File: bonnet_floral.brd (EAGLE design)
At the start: 65 x 30 mm, 10 parts, among them IC1 RASPBERRY_PI_ZERO_W_(V1.3)-WO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

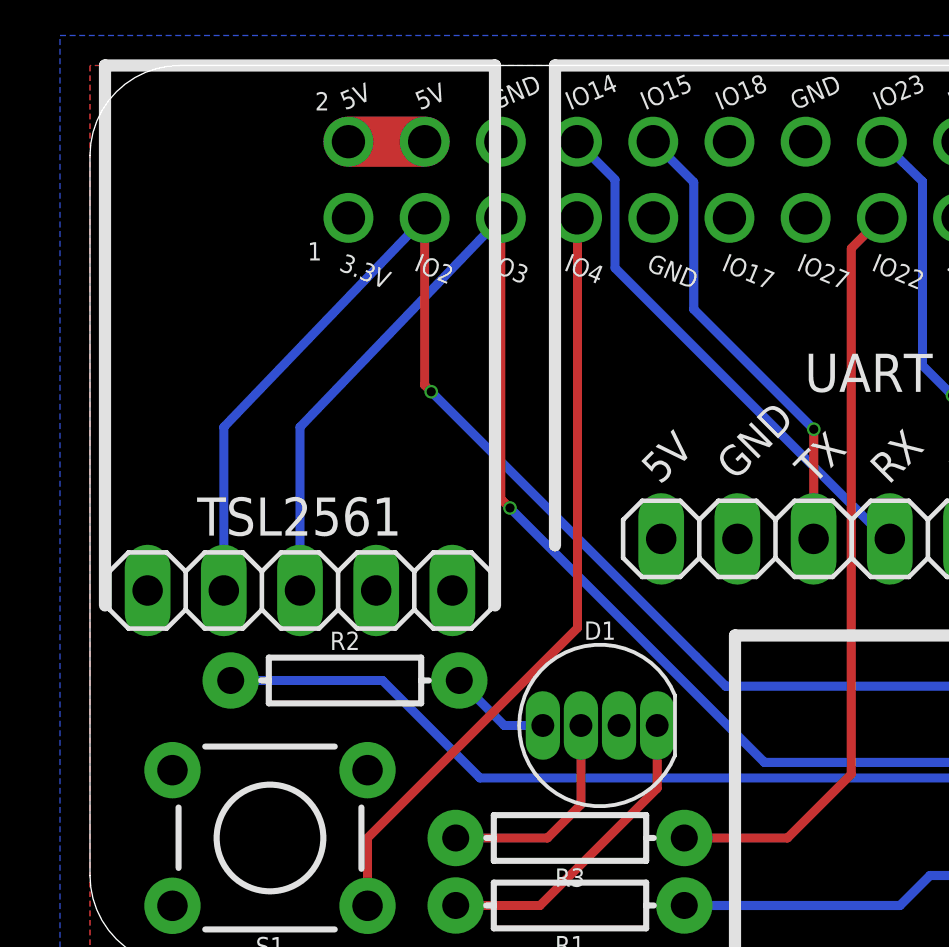
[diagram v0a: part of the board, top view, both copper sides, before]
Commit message: Adjusting the back silkscreen, adding artwork
Also cleaning up the DRC checks from before
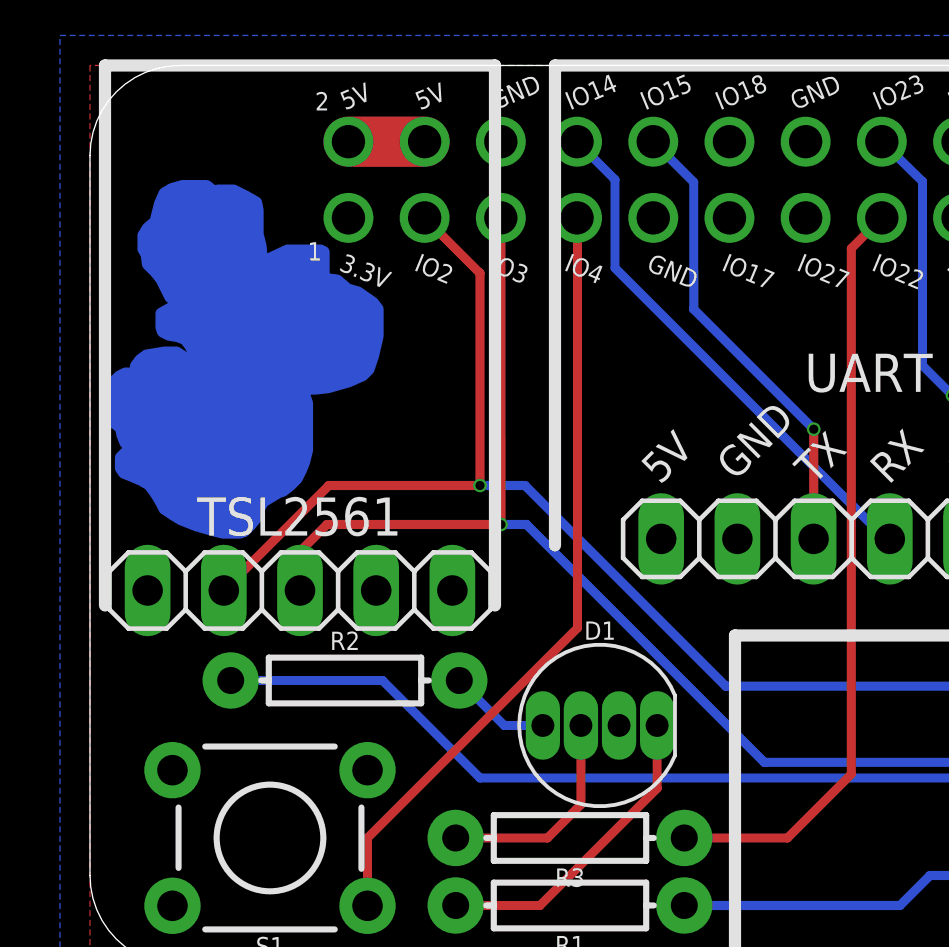
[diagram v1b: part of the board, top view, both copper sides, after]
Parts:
- added U$1: (no value), Artwork:FLORAL_SMALLER_MIRROR
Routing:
- net I2C_SCL: track 48.9 -> 42.7 mm
- net I2C_SDA: track 48.2 -> 43.9 mm
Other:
- board text added: "Floral Bonnet V0.9.1 John 'Warthog9' Hawley (C) 2018 CC-BY-SA 4.0"
- board text added: "https://github.com/unreproducible/bonnet_floral"
- board text removed: "Floral Bonnet V0.9.1 John 'Warthog9' Hawley (C) 2018 CC-BY-SA 4.0 https://github.com/unreproducible/bonnet_floral"
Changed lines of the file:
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@@
 <setting verticaltext="up"/>
 </settings>
-<grid distance="1" unitdist="mm" unit="mm" style="lines" multiple="1" display="no" altdistance="0.5" altunitdist="mm" altunit="mm"/>
+<grid distance="0.0025" unitdist="inch" unit="inch" style="lines" multiple="1" display="yes" altdistance="0.1" altunitdist="mm" altunit="mm"/>
 <layers>
 <layer number="1" name="Top" color="4" fill="1" visible="yes" active="yes"/>
@@
 <layer number="207" name="207bmp" color="8" fill="10" visible="yes" active="yes"/>
 <layer number="208" name="208bmp" color="9" fill="10" visible="yes" active="yes"/>
-<layer number="209" name="209bmp" color="7" fill="1" visible="yes" active="yes"/>
-<layer number="210" name="210bmp" color="7" fill="1" visible="yes" active="yes"/>
-<layer number="211" name="211bmp" color="7" fill="1" visible="yes" active="yes"/>
-<layer number="212" name="212bmp" color="7" fill="1" visible="yes" active="yes"/>
-<layer number="213" name="213bmp" color="7" fill="1" visible="yes" active="yes"/>
-<layer number="214" name="214bmp" color="7" fill="1" visible="yes" active="yes"/>
-<layer number="215" name="215bmp" color="7" fill="1" visible="yes" active="yes"/>
+<layer number="209" name="209bmp" color="10" fill="10" visible="yes" active="yes"/>
+<layer number="210" name="210bmp" color="11" fill="10" visible="yes" active="yes"/>
+<layer number="211" name="211bmp" color="12" fill="10" visible="yes" active="yes"/>
+<layer number="212" name="212bmp" color="13" fill="10" visible="yes" active="yes"/>
+<layer number="213" name="213bmp" color="14" fill="10" visible="yes" active="yes"/>
+<layer number="214" name="214bmp" color="15" fill="10" visible="yes" active="yes"/>
+<layer number="215" name="215bmp" color="16" fill="10" visible="yes" active="yes"/>
 <layer number="216" name="216bmp" color="7" fill="1" visible="yes" active="yes"/>
 <layer number="217" name="217bmp" color="18" fill="1" visible="no" active="no"/>
@@
 <wire x1="37.5" y1="1" x2="37.5" y2="4.75" width="0.4064" layer="21"/>
 <wire x1="37.5" y1="24" x2="37.5" y2="28.5" width="0.4064" layer="21"/>
-<text x="62" y="16" size="0.7" layer="22" rot="MR90" align="center">Floral Bonnet V0.9.1
+<text x="50.5" y="7.5" size="1.27" layer="22" rot="MR0" align="center">Floral Bonnet V0.9.1
 John 'Warthog9' Hawley
-(C) 2018 CC-BY-SA 4.0
-https://github.com/unreproducible/bonnet_floral</text>
-<text x="55" y="12" size="1.016" layer="22" rot="MR270" align="center">Specifically Designed for:
+(C) 2018 CC-BY-SA 4.0</text>
+<text x="52" y="19" size="1.27" layer="22" rot="MR180" align="center">Specifically Designed for:
 E-ALE https://e-ale.org/
 for linux.conf.au 2019</text>
@@
 <text x="29.25" y="16" size="1.016" layer="22" rot="MR45">DTR</text>
 <text x="31.75" y="16.125" size="1.016" layer="22" rot="MR45">3.3V</text>
+<text x="51.5" y="4" size="0.9" layer="22" rot="MR0" align="center">https://github.com/unreproducible/bonnet_floral</text>
 </plain>
 <attributes>
@@
 <attribute name="PROD_ID" value=" " x="16" y="4.25" size="1.778" layer="27" rot="R180" display="off"/>
 </element>
+<element name="U$1" library="Artwork" package="FLORAL_SMALLER_MIRROR" value="" x="5.134" y="20.2295" rot="MR0"/>
 </elements>
 <signals>
@@
 <contactref element="BME280" pad="2"/>
 <contactref element="IC1" pad="5-IO3"/>
-<wire x1="13.695" y1="24.92" x2="7" y2="17.945" width="0.3" layer="16"/>
-<wire x1="7" y1="17.945" x2="7" y2="12.5" width="0.3" layer="16"/>
-<wire x1="21.48" y1="7.77" x2="14" y2="15.25" width="0.3" layer="16"/>
-<via x="14" y="15.25" extent="1-16" drill="0.3048"/>
-<wire x1="14" y1="15.25" x2="13.695" y2="15.555" width="0.3" layer="1"/>
-<wire x1="13.695" y1="15.555" x2="13.695" y2="24.92" width="0.3" layer="1"/>
-<wire x1="21.48" y1="7.77" x2="22.48" y2="6.77" width="0.3048" layer="16"/>
 <wire x1="22.48" y1="6.77" x2="34.5" y2="6.77" width="0.3048" layer="16"/>
+<wire x1="13.695" y1="24.92" x2="13.7" y2="14.7" width="0.3048" layer="1"/>
+<via x="13.7" y="14.7" extent="1-16" drill="0.3048"/>
+<wire x1="7" y1="12.5" x2="7" y2="13.8" width="0.3048" layer="1"/>
+<wire x1="7" y1="13.8" x2="7.9" y2="14.7" width="0.3048" layer="1"/>
+<wire x1="7.9" y1="14.7" x2="13.7" y2="14.7" width="0.3048" layer="1"/>
+<wire x1="22.48" y1="6.77" x2="14.55" y2="14.7" width="0.3048" layer="16"/>
+<wire x1="14.55" y1="14.7" x2="13.7" y2="14.7" width="0.3048" layer="16"/>
 </signal>
 <signal name="I2C_SDA">
@@
 <contactref element="BME280" pad="1"/>
 <contactref element="IC1" pad="3-IO2"/>
-<wire x1="11.155" y1="24.92" x2="4.46" y2="17.945" width="0.3" layer="16"/>
-<wire x1="4.46" y1="17.945" x2="4.46" y2="12.5" width="0.3" layer="16"/>
-<wire x1="20.19" y1="10.31" x2="11.375" y2="19.125" width="0.3" layer="16"/>
-<wire x1="11.155" y1="24.92" x2="11.155" y2="19.345" width="0.3" layer="1"/>
-<wire x1="11.155" y1="19.345" x2="11.375" y2="19.125" width="0.3" layer="1"/>
-<via x="11.375" y="19.125" extent="1-16" drill="0.3048"/>
-<wire x1="20.19" y1="10.31" x2="21.19" y2="9.31" width="0.3048" layer="16"/>
 <wire x1="21.19" y1="9.31" x2="34.5" y2="9.31" width="0.3048" layer="16"/>
+<wire x1="11.155" y1="24.92" x2="13" y2="23.075" width="0.3048" layer="1"/>
+<wire x1="13" y1="23.075" x2="13" y2="16" width="0.3048" layer="1"/>
+<via x="13" y="16" extent="1-16" drill="0.3048"/>
+<wire x1="4.46" y1="12.5" x2="7.96" y2="16" width="0.3048" layer="1"/>
+<wire x1="7.96" y1="16" x2="13" y2="16" width="0.3048" layer="1"/>
+<wire x1="21.19" y1="9.31" x2="14.5" y2="16" width="0.3048" layer="16"/>
+<wire x1="14.5" y1="16" x2="13" y2="16" width="0.3048" layer="16"/>
 </signal>
 <signal name="TSL_INT">
@@
 <contactref element="UART" pad="1"/>
 </signal>
+<signal name="N$4">
+</signal>
 </signals>
